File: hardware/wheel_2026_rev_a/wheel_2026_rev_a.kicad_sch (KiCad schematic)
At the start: 15 parts, among them J2 RPI, U1 TCRT5000, U3 MLX90614xSF-AxA-000-TU, U4 TLV2372IDR

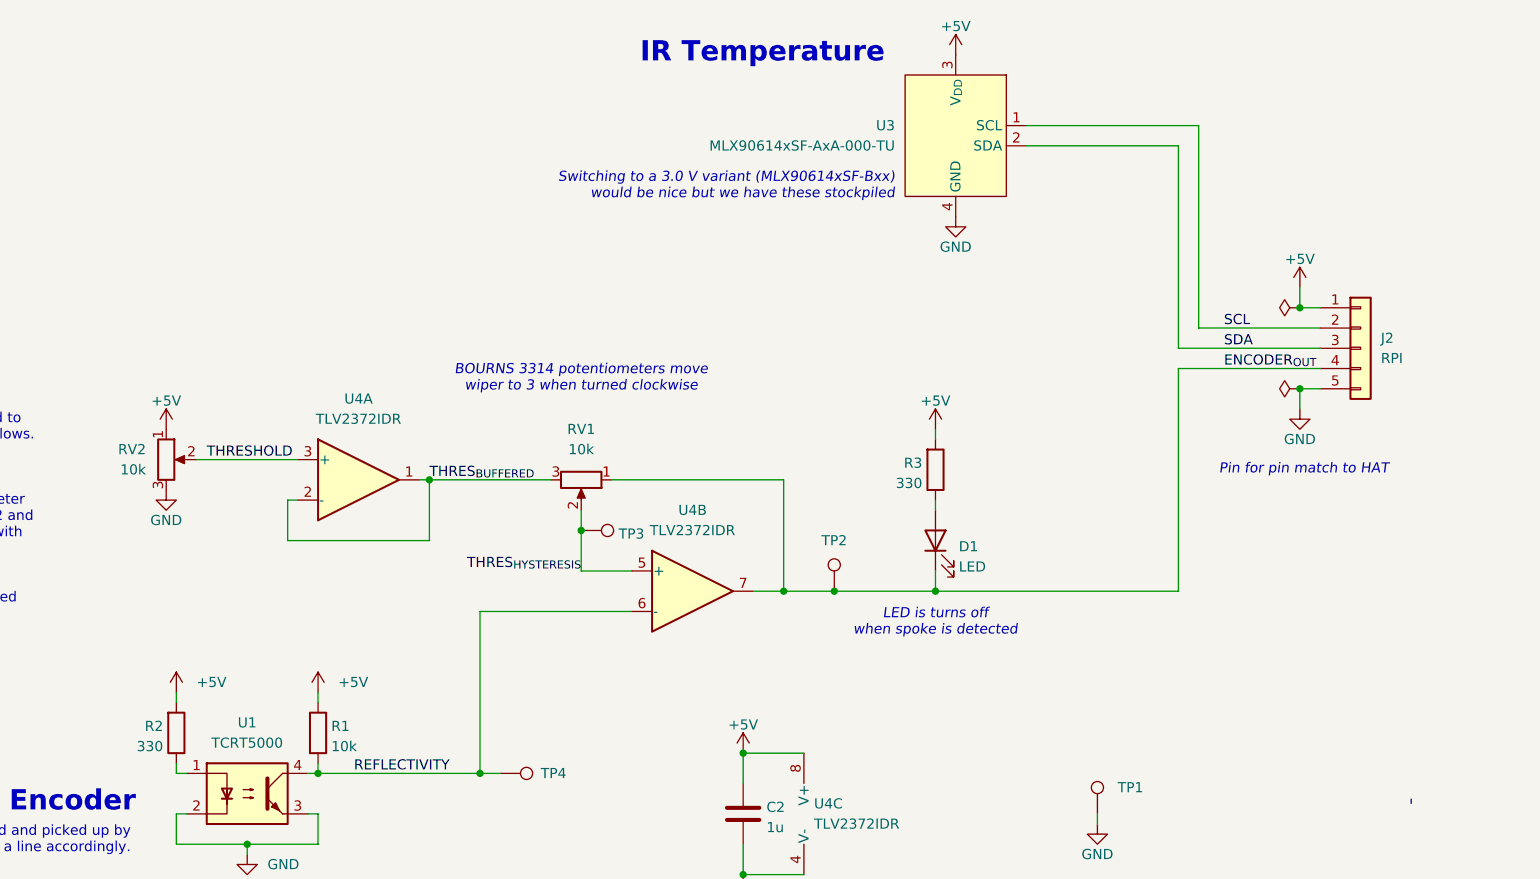
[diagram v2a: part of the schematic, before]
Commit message: Wheel rev A PCB as ordered
Added note to use 3.3V power but 5V was endured before without issue.
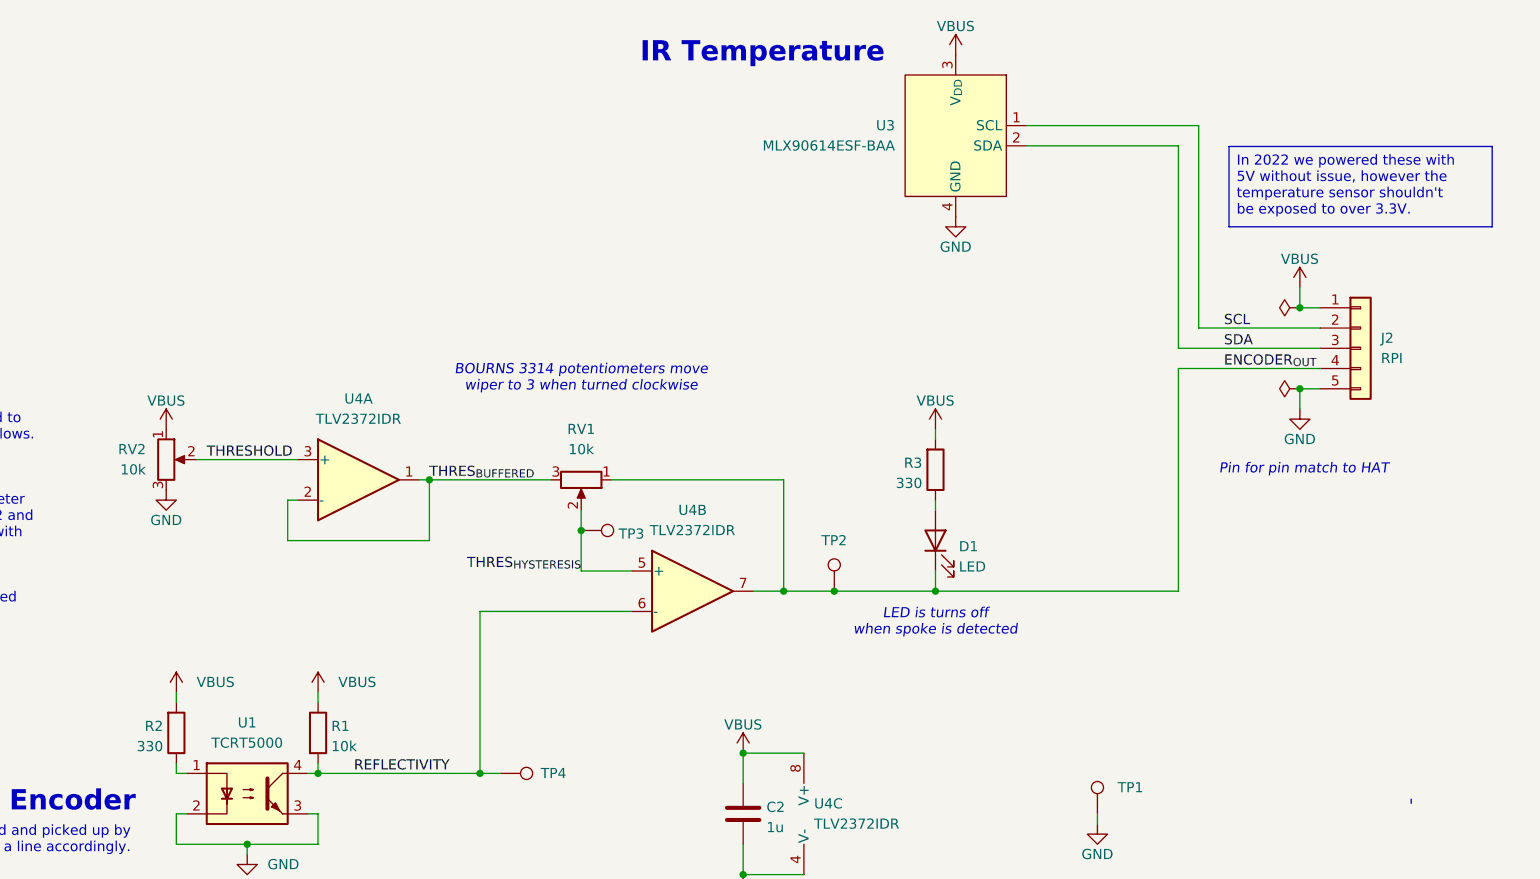
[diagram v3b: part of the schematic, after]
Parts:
- U3: value MLX90614xSF-AxA-000-TU -> MLX90614ESF-BAA; LCSC (none) -> C490604
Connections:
- net +5V renamed VBUS
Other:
- note removed: "Switching to a 3.0 V variant (MLX90614xSF-Bxx) would be nice but we have these stockpiled"
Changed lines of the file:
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@@
 		)
 	)
-	(text "Switching to a 3.0 V variant (MLX90614xSF-Bxx)\nwould be nice but we have these stockpiled\n"
-		(exclude_from_sim no)
-		(at 187.96 62.23 0)
-		(effects
-			(font
-				(size 1.27 1.27)
-				(italic yes)
-			)
-			(justify right)
-		)
-	)
 	(text_box "Two stage op-amp circuit. The threshold voltage is buffered to prevent loading effects from the hysteresis division that follows. Hysteresis is used to prevent spurrious switching near the threshold.\n\nFirst set the threshold, by setting the hysteresis potentiometer to entirely favour the threshold value (short between pins 2 and 3 on RV1) before probing TP3 and adjusting the threshold with RV2 - it should be about halfway through the reflectivity signal's range as the wheel rotates past it.\n\nOnce the threshold is set, adjust RV1 to introduce the desired level of hysteresis."
 		(exclude_from_sim no)
@@
 		)
 	)
+	(text_box "In 2022 we powered these with 5V without issue, however the temperature sensor shouldn't be exposed to over 3.3V."
+		(exclude_from_sim no)
+		(at 229.87 57.2278 0)
+		(size 33.02 10.0822)
+		(margins 0.9525 0.9525 0.9525 0.9525)
+		(stroke
+			(width 0)
+			(type solid)
+		)
+		(fill
+			(type none)
+		)
+		(effects
+			(font
+				(size 1.27 1.27)
+			)
+			(justify left top)
+		)
+	)
 	(junction
 		(at 173.99 113.03)
@@
 	)
 	(symbol
-		(lib_id "power:+5V")
+		(lib_id "power:VBUS")
 		(at 97.79 125.73 0)
 		(unit 1)
@@
 			)
 		)
-		(property "Value" "+5V"
+		(property "Value" "VBUS"
 			(at 100.33 124.4599 0)
 			(show_name no)
@@
 			)
 		)
-		(property "Description" "Power symbol creates a global label with name \"+5V\""
+		(property "Description" "Power symbol creates a global label with name \"VBUS\""
 			(at 97.79 125.73 0)
 			(hide yes)
@@
 			)
 		)
-		(property "Value" "MLX90614xSF-AxA-000-TU"
+		(property "Value" "MLX90614ESF-BAA"
 			(at 187.96 57.1499 0)
 			(show_name no)
@@
 			)
 		)
+		(property "LCSC" "C490604"
+			(at 195.58 55.88 0)
+			(hide yes)
+			(show_name no)
+			(do_not_autoplace no)
+			(effects
+				(font
+					(size 1.27 1.27)
+				)
+			)
+		)
 		(pin "1"
 		)
@@
 	)
 	(symbol
-		(lib_id "power:+5V")
+		(lib_id "power:VBUS")
 		(at 96.52 92.71 0)
 		(mirror y)
@@
 			)
 		)
-		(property "Value" "+5V"
+		(property "Value" "VBUS"
 			(at 96.52 89.154 0)
 			(show_name no)
@@
 			)
 		)
-		(property "Description" "Power symbol creates a global label with name \"+5V\""
+		(property "Description" "Power symbol creates a global label with name \"VBUS\""
 			(at 96.52 92.71 0)
 			(hide yes)
@@
 			)
 		)
-		(property "Datasheet" ""
+		(property "Datasheet" "https://www.vishay.com/docs/83760/tcrt5000.pdf"
 			(at 106.68 138.43 0)
 			(hide yes)
@@
 	)
 	(symbol
-		(lib_id "power:+5V")
+		(lib_id "power:VBUS")
 		(at 168.91 133.35 0)
 		(mirror y)
@@
 			)
 		)
-		(property "Value" "+5V"
+		(property "Value" "VBUS"
 			(at 168.91 129.794 0)
 			(show_name no)
@@
 			)
 		)
-		(property "Description" "Power symbol creates a global label with name \"+5V\""
+		(property "Description" "Power symbol creates a global label with name \"VBUS\""
 			(at 168.91 133.35 0)
 			(hide yes)
@@
 	)
 	(symbol
-		(lib_id "power:+5V")
+		(lib_id "power:VBUS")
 		(at 195.58 45.72 0)
 		(unit 1)
@@
 			)
 		)
-		(property "Value" "+5V"
+		(property "Value" "VBUS"
 			(at 195.58 42.164 0)
 			(show_name no)
@@
 			)
 		)
-		(property "Description" "Power symbol creates a global label with name \"+5V\""
+		(property "Description" "Power symbol creates a global label with name \"VBUS\""
 			(at 195.58 45.72 0)
 			(hide yes)
@@
 	)
 	(symbol
-		(lib_id "power:+5V")
+		(lib_id "power:VBUS")
 		(at 193.04 92.71 0)
 		(mirror y)
@@
 			)
 		)
-		(property "Value" "+5V"
+		(property "Value" "VBUS"
 			(at 193.04 89.154 0)
 			(show_name no)
@@
 			)
 		)
-		(property "Description" "Power symbol creates a global label with name \"+5V\""
+		(property "Description" "Power symbol creates a global label with name \"VBUS\""
 			(at 193.04 92.71 0)
 			(hide yes)
@@
 	)
 	(symbol
-		(lib_id "power:+5V")
+		(lib_id "power:VBUS")
 		(at 238.76 74.93 0)
 		(unit 1)
@@
 			)
 		)
-		(property "Value" "+5V"
+		(property "Value" "VBUS"
 			(at 238.76 71.374 0)
 			(show_name no)
@@
 			)
 		)
-		(property "Description" "Power symbol creates a global label with name \"+5V\""
+		(property "Description" "Power symbol creates a global label with name \"VBUS\""
 			(at 238.76 74.93 0)
 			(hide yes)
@@
 	)
 	(symbol
-		(lib_id "power:+5V")
+		(lib_id "power:VBUS")
 		(at 115.57 125.73 0)
 		(mirror y)
@@
 			)
 		)
-		(property "Value" "+5V"
+		(property "Value" "VBUS"
 			(at 118.11 124.4599 0)
 			(show_name no)
@@
 			)
 		)
-		(property "Description" "Power symbol creates a global label with name \"+5V\""
+		(property "Description" "Power symbol creates a global label with name \"VBUS\""
 			(at 115.57 125.73 0)
 			(hide yes)
